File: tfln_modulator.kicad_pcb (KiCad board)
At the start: 4 copper layers, 1 part

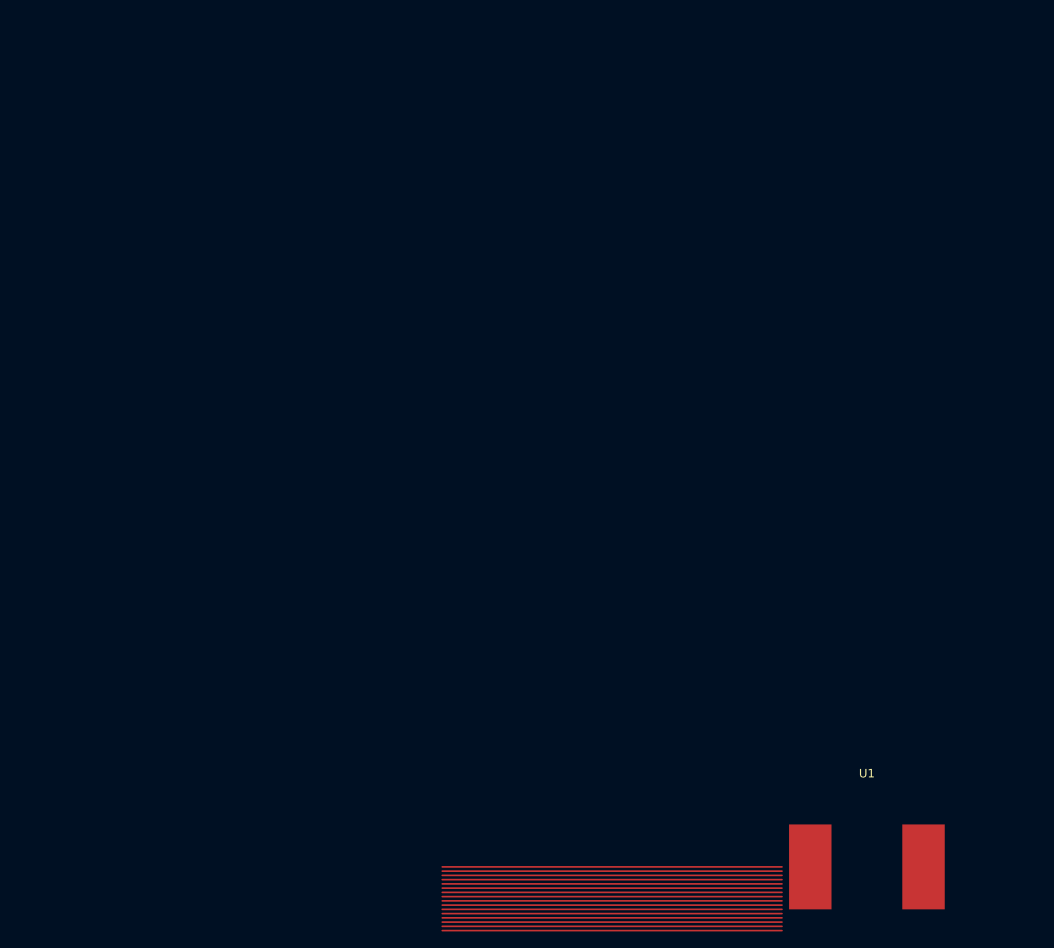
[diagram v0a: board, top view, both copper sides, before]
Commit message: Enhanced KiCad design with full BOM components, nets, and 12-layer stackup
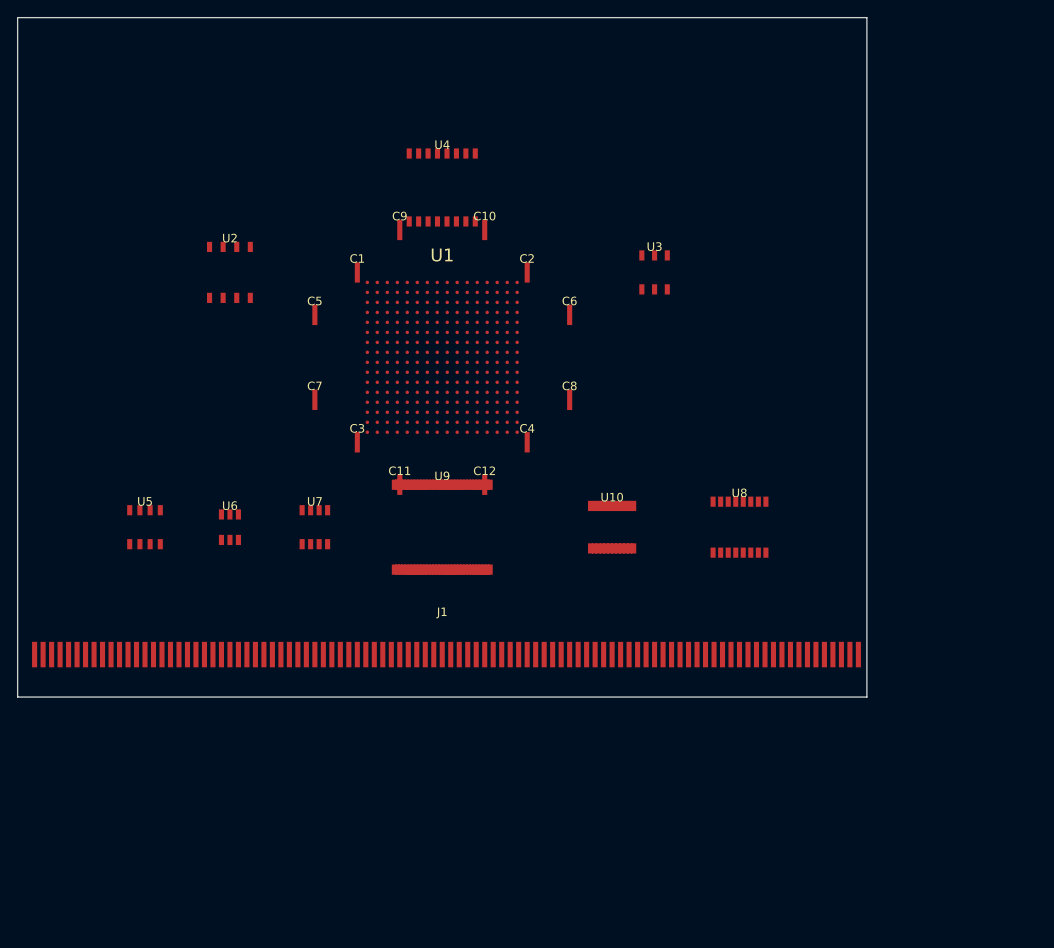
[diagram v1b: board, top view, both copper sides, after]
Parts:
- added C1: 10uF, Package_SO:SOIC-2, F.Cu at (40.0, 30.0)
- added C10: 10uF, Package_SO:SOIC-2, F.Cu at (55.0, 25.0)
- added C11: 10uF, Package_SO:SOIC-2, F.Cu at (45.0, 55.0)
- added C12: 10uF, Package_SO:SOIC-2, F.Cu at (55.0, 55.0)
- added C2: 10uF, Package_SO:SOIC-2, F.Cu at (60.0, 30.0)
- added C3: 10uF, Package_SO:SOIC-2, F.Cu at (40.0, 50.0)
- added C4: 10uF, Package_SO:SOIC-2, F.Cu at (60.0, 50.0)
- added C5: 10uF, Package_SO:SOIC-2, F.Cu at (35.0, 35.0)
- added C6: 10uF, Package_SO:SOIC-2, F.Cu at (65.0, 35.0)
- added C7: 10uF, Package_SO:SOIC-2, F.Cu at (35.0, 45.0)
- added C8: 10uF, Package_SO:SOIC-2, F.Cu at (65.0, 45.0)
- added C9: 10uF, Package_SO:SOIC-2, F.Cu at (45.0, 25.0)
- added J1: , Connector_PCIe:PCIe_x16, F.Cu at (50.0, 75.0)
- added U10: Si5395A, Package_SO:SOIC-24, F.Cu at (70.0, 60.0)
- added U2: TLN-1550-100, Package_SO:SOIC-8, F.Cu at (25.0, 30.0)
- added U3: XPDV4120R, Package_SO:SOIC-6, F.Cu at (75.0, 30.0)
- added U4: HMC8410, Package_SO:SOIC-16, F.Cu at (50.0, 20.0)
- added U5: MAX3669, Package_SO:SOIC-8, F.Cu at (15.0, 60.0)
- added U6: TPS7A4700, Package_SO:SOIC-6, F.Cu at (25.0, 60.0)
- added U7: LT8614, Package_SO:SOIC-8, F.Cu at (35.0, 60.0)
- added U8: MPT5000, Package_SO:SOIC-16, F.Cu at (85.0, 60.0)
- added U9: BCM84881, Package_SO:SOIC-64, F.Cu at (50.0, 60.0)
- U1: footprint ManualPkg:U1 -> Package_BGA:BGA-256
- moved U1 78.1 mm to (50.0, 40.0)
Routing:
- net (no net): track 640.0 -> 0.00 mm
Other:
- board outline added: 100 x 80 mm
- copper layers 4 -> 12

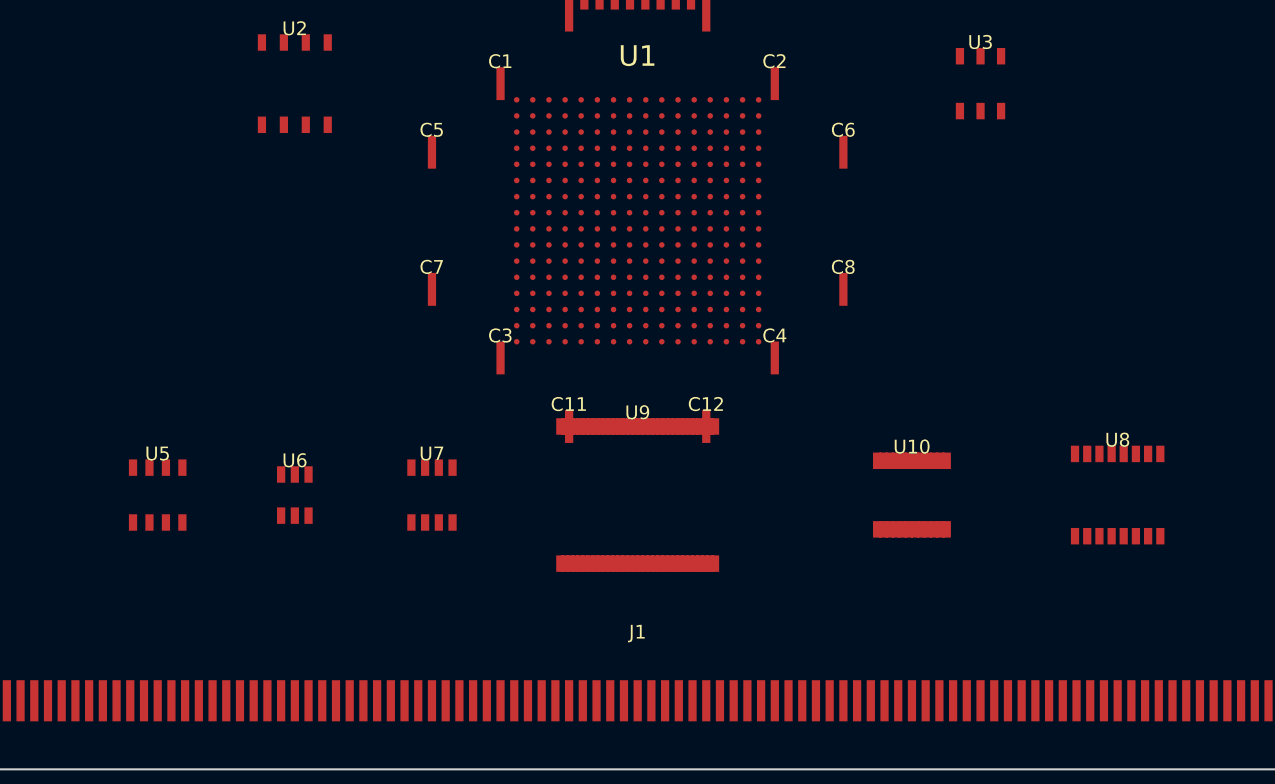
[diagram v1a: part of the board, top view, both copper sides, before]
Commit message: Add routing traces, EasyEDA export, and comprehensive README
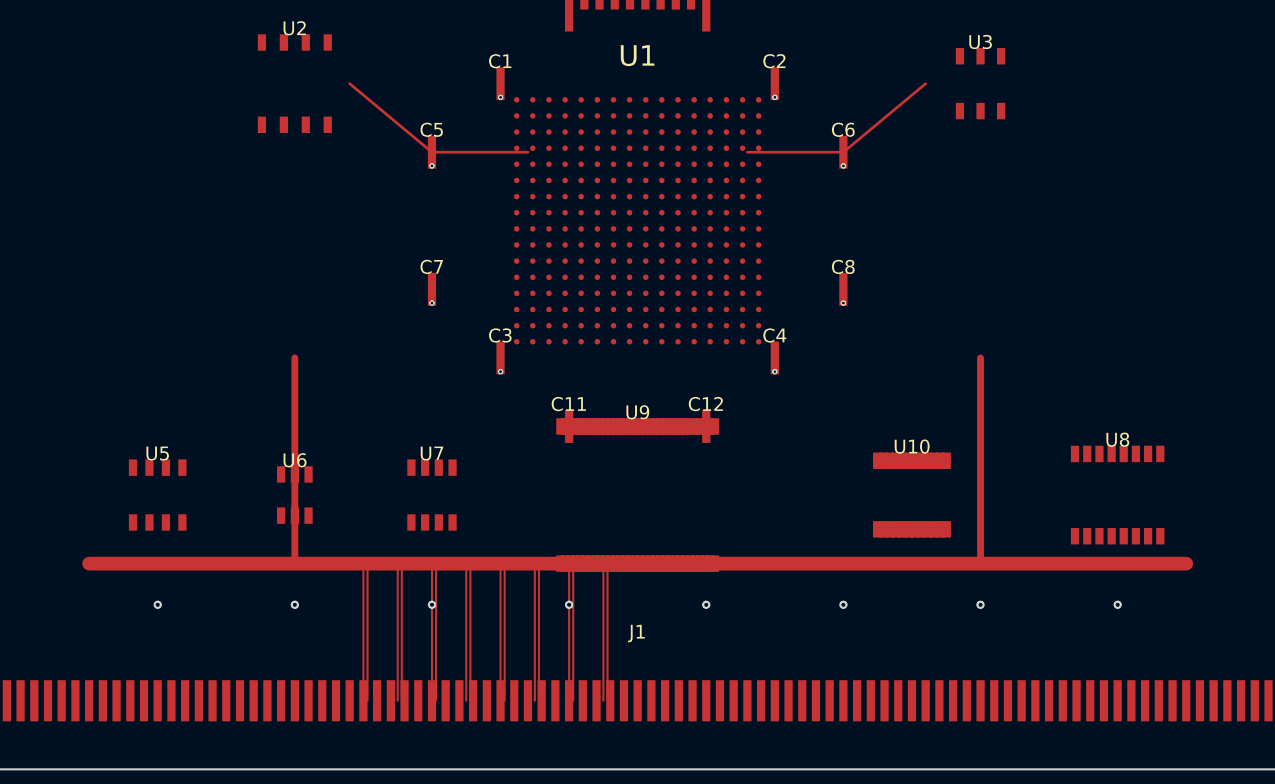
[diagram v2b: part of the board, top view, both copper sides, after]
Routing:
- net +3V3: track 0.00 -> 110.0 mm
- net PD_OUT: track 0.00 -> 14.8 mm
- net LASER_EN: track 0.00 -> 14.8 mm
- net PCIE7_TX_P: track 0.00 -> 10.0 mm
- net PCIE7_TX_N: track 0.00 -> 10.0 mm
- net PCIE6_TX_P: track 0.00 -> 10.0 mm
- net PCIE6_TX_N: track 0.00 -> 10.0 mm
- net PCIE5_TX_P: track 0.00 -> 10.0 mm
- net PCIE5_TX_N: track 0.00 -> 10.0 mm
- net PCIE4_TX_P: track 0.00 -> 10.0 mm
- net PCIE4_TX_N: track 0.00 -> 10.0 mm
- net PCIE3_TX_P: track 0.00 -> 10.0 mm
- net PCIE3_TX_N: track 0.00 -> 10.0 mm
- net PCIE2_TX_P: track 0.00 -> 10.0 mm
- net PCIE2_TX_N: track 0.00 -> 10.0 mm
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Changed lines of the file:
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@@
     (pad "98" smd rect (at 49 0) (size 0.6 3) (layers "F.Cu" "F.Paste" "F.Mask") (net 0 ""))
   )
+  (segment (start 10 65) (end 90 65) (width 1.0) (layer "F.Cu") (net 2))
+  (segment (start 25 65) (end 25 50) (width 0.5) (layer "F.Cu") (net 2))
+  (segment (start 75 65) (end 75 50) (width 0.5) (layer "F.Cu") (net 2))
+  (via (at 15 68) (size 0.6) (drill 0.3) (layers "F.Cu" "B.Cu") (net 1))
+  (via (at 25 68) (size 0.6) (drill 0.3) (layers "F.Cu" "B.Cu") (net 1))
+  (via (at 35 68) (size 0.6) (drill 0.3) (layers "F.Cu" "B.Cu") (net 1))
+  (via (at 45 68) (size 0.6) (drill 0.3) (layers "F.Cu" "B.Cu") (net 1))
+  (via (at 55 68) (size 0.6) (drill 0.3) (layers "F.Cu" "B.Cu") (net 1))
+  (via (at 65 68) (size 0.6) (drill 0.3) (layers "F.Cu" "B.Cu") (net 1))
+  (via (at 75 68) (size 0.6) (drill 0.3) (layers "F.Cu" "B.Cu") (net 1))
+  (via (at 85 68) (size 0.6) (drill 0.3) (layers "F.Cu" "B.Cu") (net 1))
+  (segment (start 29 30) (end 35 35) (width 0.2) (layer "F.Cu") (net 70))
+  (segment (start 35 35) (end 42 35) (width 0.2) (layer "F.Cu") (net 70))
+  (segment (start 58 35) (end 65 35) (width 0.2) (layer "F.Cu") (net 72))
+  (segment (start 65 35) (end 71 30) (width 0.2) (layer "F.Cu") (net 72))
+  (segment (start 30.0 75) (end 30.0 65) (width 0.15) (layer "F.Cu") (net 6))
+  (segment (start 30.3 75) (end 30.3 65) (width 0.15) (layer "F.Cu") (net 7))
+  (segment (start 32.5 75) (end 32.5 65) (width 0.15) (layer "F.Cu") (net 10))
+  (segment (start 32.8 75) (end 32.8 65) (width 0.15) (layer "F.Cu") (net 11))
+  (segment (start 35.0 75) (end 35.0 65) (width 0.15) (layer "F.Cu") (net 14))
+  (segment (start 35.3 75) (end 35.3 65) (width 0.15) (layer "F.Cu") (net 15))
+  (segment (start 37.5 75) (end 37.5 65) (width 0.15) (layer "F.Cu") (net 18))
+  (segment (start 37.8 75) (end 37.8 65) (width 0.15) (layer "F.Cu") (net 19))
+  (segment (start 40.0 75) (end 40.0 65) (width 0.15) (layer "F.Cu") (net 22))
+  (segment (start 40.3 75) (end 40.3 65) (width 0.15) (layer "F.Cu") (net 23))
+  (segment (start 42.5 75) (end 42.5 65) (width 0.15) (layer "F.Cu") (net 26))
+  (segment (start 42.8 75) (end 42.8 65) (width 0.15) (layer "F.Cu") (net 27))
+  (segment (start 45.0 75) (end 45.0 65) (width 0.15) (layer "F.Cu") (net 30))
+  (segment (start 45.3 75) (end 45.3 65) (width 0.15) (layer "F.Cu") (net 31))
+  (segment (start 47.5 75) (end 47.5 65) (width 0.15) (layer "F.Cu") (net 34))
+  (segment (start 47.8 75) (end 47.8 65) (width 0.15) (layer "F.Cu") (net 35))
+  (via (at 40 31) (size 0.4) (drill 0.2) (layers "F.Cu" "B.Cu") (net 1))
+  (via (at 60 31) (size 0.4) (drill 0.2) (layers "F.Cu" "B.Cu") (net 1))
+  (via (at 40 51) (size 0.4) (drill 0.2) (layers "F.Cu" "B.Cu") (net 1))
+  (via (at 60 51) (size 0.4) (drill 0.2) (layers "F.Cu" "B.Cu") (net 1))
+  (via (at 35 36) (size 0.4) (drill 0.2) (layers "F.Cu" "B.Cu") (net 1))
+  (via (at 65 36) (size 0.4) (drill 0.2) (layers "F.Cu" "B.Cu") (net 1))
+  (via (at 35 46) (size 0.4) (drill 0.2) (layers "F.Cu" "B.Cu") (net 1))
+  (via (at 65 46) (size 0.4) (drill 0.2) (layers "F.Cu" "B.Cu") (net 1))
 )

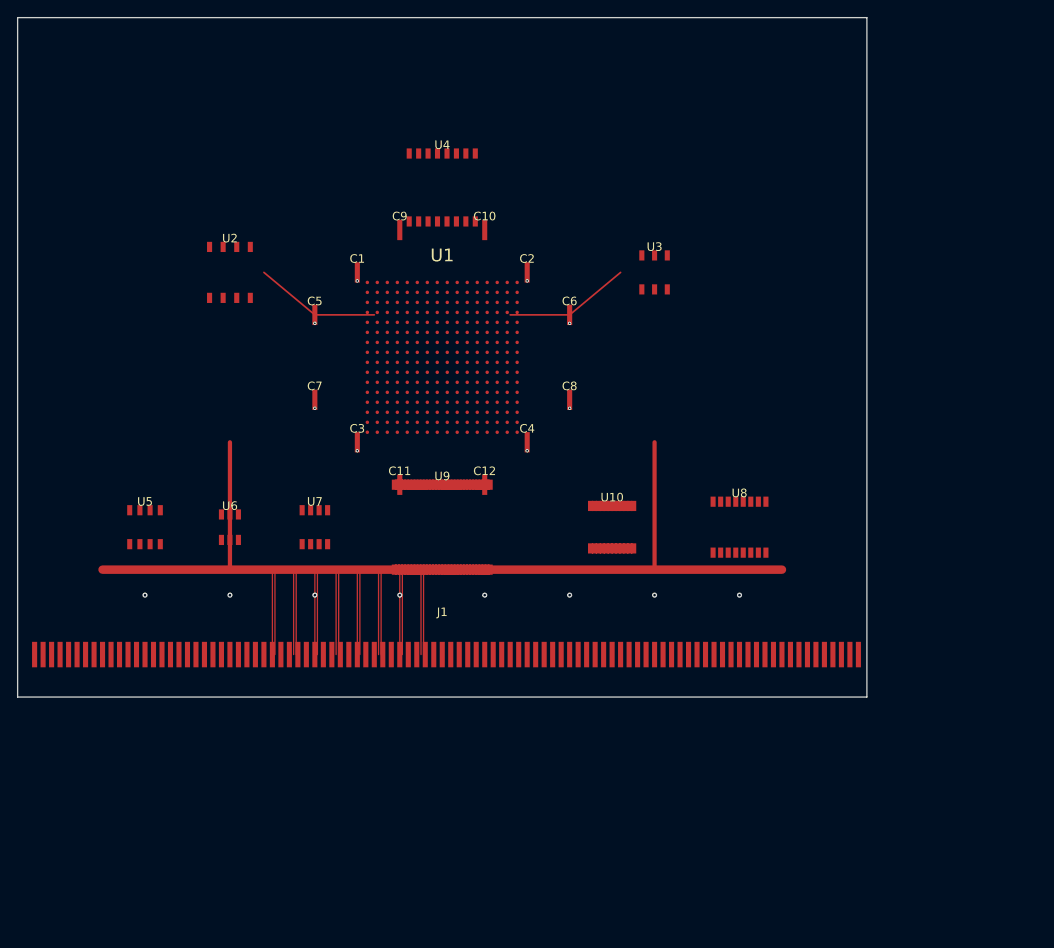
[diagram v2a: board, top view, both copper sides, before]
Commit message: Fix KiCad design: proper net assignments and non-overlapping pads for DeepPCB
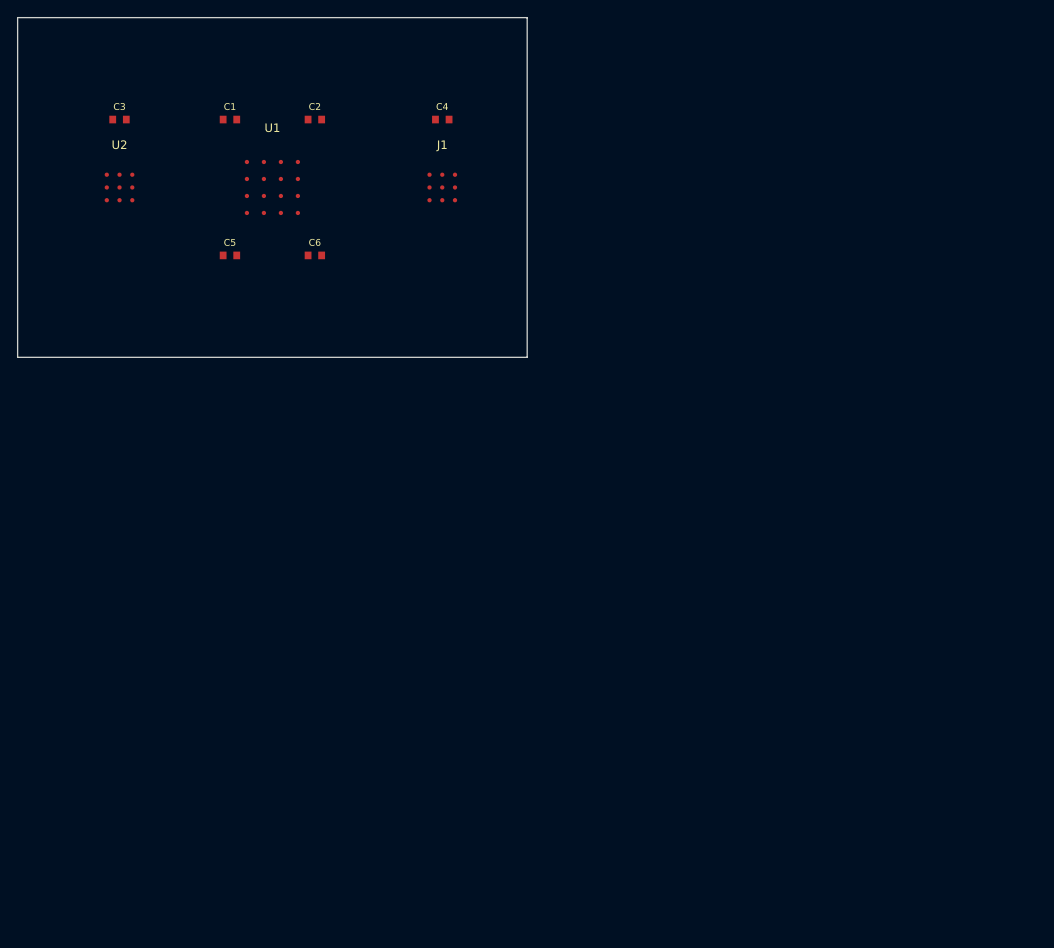
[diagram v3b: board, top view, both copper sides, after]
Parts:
- removed C10, C11, C12, C7, C8, C9: 10uF, Package_SO:SOIC-2
- removed U10: Si5395A, Package_SO:SOIC-24
- removed U3: XPDV4120R, Package_SO:SOIC-6
- removed U4: HMC8410, Package_SO:SOIC-16
- removed U5: MAX3669, Package_SO:SOIC-8
- removed U6: TPS7A4700, Package_SO:SOIC-6
- removed U7: LT8614, Package_SO:SOIC-8
- removed U8: MPT5000, Package_SO:SOIC-16
- removed U9: BCM84881, Package_SO:SOIC-64
- C1, C2, C3, C4, C5, C6: value 10uF -> (none); footprint Package_SO:SOIC-2 -> Capacitor_SMD:C_0603
- J1: footprint Connector_PCIe:PCIe_x16 -> Custom:J1
- U1: footprint Package_BGA:BGA-256 -> Custom:U1
- U2: value TLN-1550-100 -> (none); footprint Package_SO:SOIC-8 -> Custom:U2
- moved J1 55.0 mm to (50.0, 20.0)
- moved C3 47.2 mm to (12.0, 12.0)
- moved C4 39.3 mm to (50.0, 12.0)
- moved C2 30.8 mm to (35.0, 12.0)
- moved C6 30.8 mm to (35.0, 28.0)
- moved U1 28.3 mm to (30.0, 20.0)
- moved C1 23.4 mm to (25.0, 12.0)
- moved U2 16.4 mm to (12.0, 20.0)
- moved C5 12.2 mm to (25.0, 28.0)
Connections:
- C1 pad 1: (no net) -> VCC
- C1 pad 2: (no net) -> GND
- C2 pad 1: (no net) -> +3V3
- C2 pad 2: (no net) -> GND
- C3 pad 1: (no net) -> VCC
- C3 pad 2: (no net) -> GND
- C4 pad 1: (no net) -> VCC
- C4 pad 2: (no net) -> GND
- C5 pad 1: (no net) -> SIG6
- C5 pad 2: (no net) -> GND
- C6 pad 1: (no net) -> SIG7
- C6 pad 2: (no net) -> GND
- J1 pad 1: (no net) -> SIG2
- J1 pad 2: (no net) -> SIG3
- J1 pad 3: (no net) -> SIG4
- J1 pad 4: (no net) -> SIG5
- J1 pad 5: (no net) -> GND
- J1 pad 6: (no net) -> VCC
- J1 pad 7: (no net) -> SIG15
- J1 pad 8: (no net) -> SIG16
- J1 pad 9: (no net) -> SIG17
- U1 pad 1: (no net) -> VCC
- U1 pad 10: (no net) -> SIG8
- U1 pad 11: (no net) -> GND
- U1 pad 12: (no net) -> VCC
- U1 pad 13: (no net) -> SIG9
- U1 pad 14: (no net) -> SIG10
- U1 pad 15: (no net) -> +3V3
- U1 pad 16: (no net) -> GND
- U1 pad 2: (no net) -> GND
- U1 pad 3: (no net) -> SIG1
- U1 pad 4: (no net) -> SIG2
- U1 pad 5: (no net) -> SIG3
- U1 pad 6: (no net) -> SIG4
- U1 pad 7: (no net) -> SIG5
- U1 pad 8: (no net) -> SIG6
- U1 pad 9: (no net) -> SIG7
- U2 pad 1: (no net) -> VCC
- U2 pad 2: (no net) -> GND
- U2 pad 3: (no net) -> SIG1
- U2 pad 4: (no net) -> SIG11
- U2 pad 5: (no net) -> SIG12
- U2 pad 6: (no net) -> SIG13
- U2 pad 7: (no net) -> +3V3
- U2 pad 8: (no net) -> GND
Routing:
- net +3V3: track 110.0 -> 0.00 mm
- net PD_OUT: track 14.8 -> 0.00 mm
- net LASER_EN: track 14.8 -> 0.00 mm
- net PCIE7_TX_P: track 10.0 -> 0.00 mm
- net PCIE7_TX_N: track 10.0 -> 0.00 mm
- net PCIE6_TX_P: track 10.0 -> 0.00 mm
- net PCIE6_TX_N: track 10.0 -> 0.00 mm
- net PCIE5_TX_P: track 10.0 -> 0.00 mm
- net PCIE5_TX_N: track 10.0 -> 0.00 mm
- net PCIE4_TX_P: track 10.0 -> 0.00 mm
- net PCIE4_TX_N: track 10.0 -> 0.00 mm
- net PCIE3_TX_P: track 10.0 -> 0.00 mm
- net PCIE3_TX_N: track 10.0 -> 0.00 mm
- net PCIE2_TX_P: track 10.0 -> 0.00 mm
- net PCIE2_TX_N: track 10.0 -> 0.00 mm
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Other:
- board size 100 x 80 mm -> 60 x 40 mm
- copper layers 12 -> 4
